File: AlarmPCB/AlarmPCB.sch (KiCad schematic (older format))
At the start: 13 parts

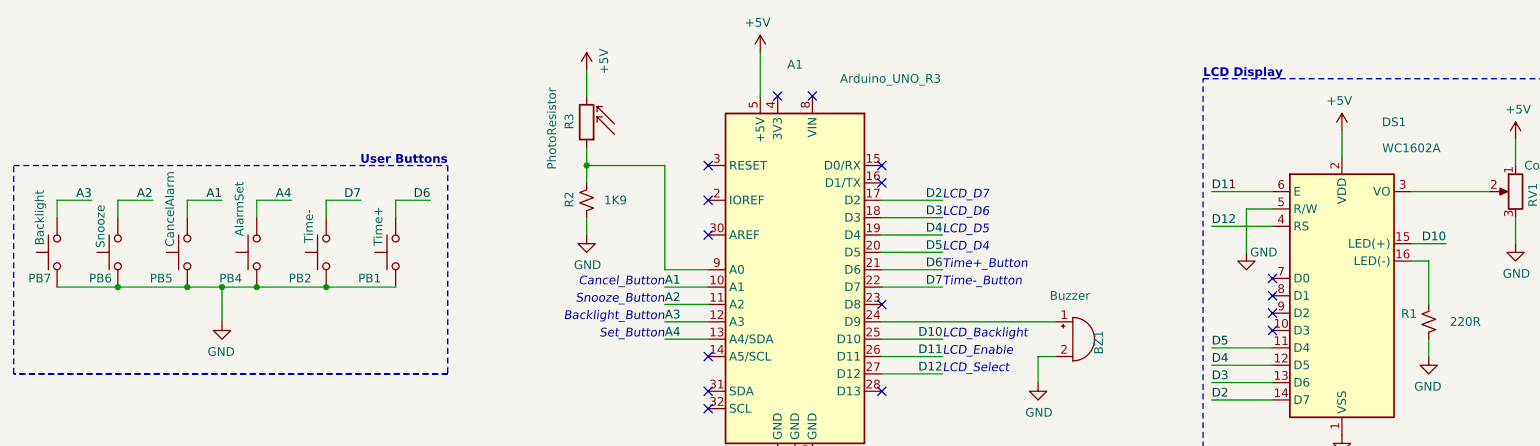
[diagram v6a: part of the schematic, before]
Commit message: Fixed push-button numbering
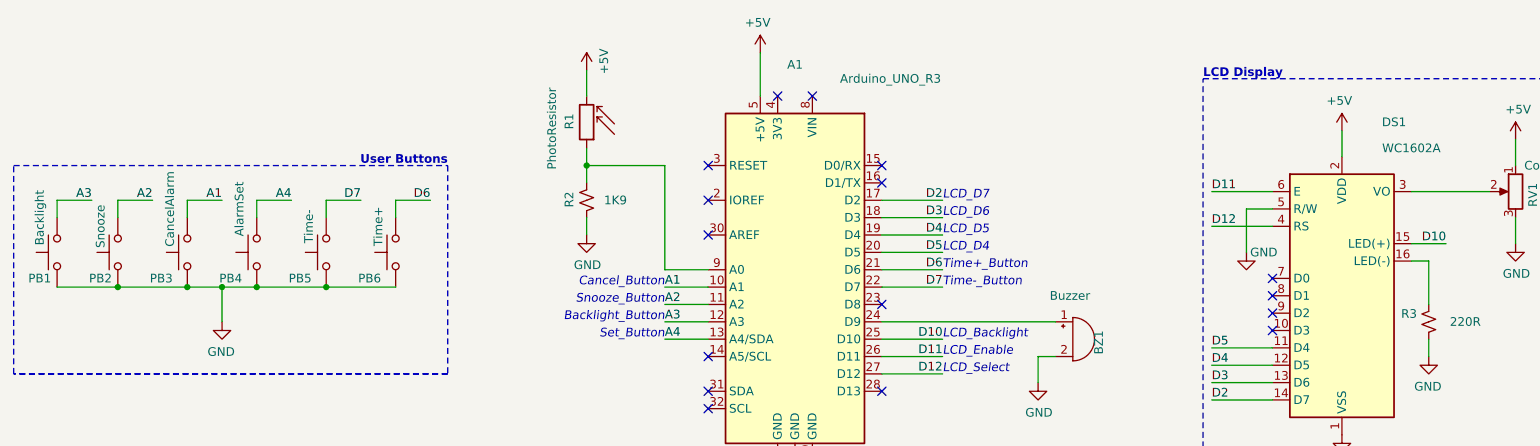
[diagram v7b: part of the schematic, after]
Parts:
- renumbered PB7 to PB1, PB6 to PB2, PB5 to PB3, PB2 to PB5, PB1 to PB6, R3 to R1, R1 to R3
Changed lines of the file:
@@
 EESchema Schematic File Version 4
+LIBS:AlarmPCB-cache
 EELAYER 30 0
 EELAYER END
@@
 $EndComp
 $Comp
-L power:GND #PWR03
+L power:GND #PWR05
 U 1 1 5EFFE387
 P 5250 5100
-F 0 "#PWR03" H 5250 4850 50  0001 C CNN
+F 0 "#PWR05" H 5250 4850 50  0001 C CNN
 F 1 "GND" H 5255 4927 50  0000 C CNN
 F 2 "" H 5250 5100 50  0001 C CNN
@@
 $EndComp
 $Comp
-L power:GND #PWR02
+L power:GND #PWR09
 U 1 1 5F06DAC4
 P 8400 4800
-F 0 "#PWR02" H 8400 4550 50  0001 C CNN
+F 0 "#PWR09" H 8400 4550 50  0001 C CNN
 F 1 "GND" H 8405 4627 50  0000 C CNN
 F 2 "" H 8400 4800 50  0001 C CNN
@@
 $EndComp
 $Comp
-L power:+5V #PWR01
+L power:+5V #PWR08
 U 1 1 5F06E403
 P 8400 3050
-F 0 "#PWR01" H 8400 2900 50  0001 C CNN
+F 0 "#PWR08" H 8400 2900 50  0001 C CNN
 F 1 "+5V" H 8415 3223 50  0000 C CNN
 F 2 "" H 8400 3050 50  0001 C CNN
@@
 	7850 3500 7850 3750
 $Comp
-L power:GND #PWR05
+L power:GND #PWR07
 U 1 1 5F070A81
 P 7850 3750
-F 0 "#PWR05" H 7850 3500 50  0001 C CNN
+F 0 "#PWR07" H 7850 3500 50  0001 C CNN
 F 1 "GND" H 7750 3750 50  0000 C CNN
 F 2 "" H 7850 3750 50  0001 C CNN
@@
 	8900 3800 8900 4050
 $Comp
-L Device:R_Small_US R1
+L Device:R_Small_US R3
 U 1 1 5F073E17
 P 8900 4150
-F 0 "R1" H 8968 4196 50  0000 L CNN
+F 0 "R3" H 8968 4196 50  0000 L CNN
 F 1 "220R" H 8600 4150 50  0000 L CNN
 F 2 "Resistor_THT:R_Axial_DIN0309_L9.0mm_D3.2mm_P12.70mm_Horizontal" H 8900 4150 50  0001 C CNN
@@
 $EndComp
 $Comp
-L power:GND #PWR07
+L power:GND #PWR010
 U 1 1 5F075220
 P 8900 4350
-F 0 "#PWR07" H 8900 4100 50  0001 C CNN
+F 0 "#PWR010" H 8900 4100 50  0001 C CNN
 F 1 "GND" H 8905 4177 50  0000 C CNN
 F 2 "" H 8900 4350 50  0001 C CNN
@@
 D2
 $Comp
-L Switch:SW_Push PB1
+L Switch:SW_Push PB6
 U 1 1 5F088DBE
 P 2950 3750
-F 0 "PB1" V 3100 3900 50  0000 C CNN
+F 0 "PB6" V 3100 3900 50  0000 C CNN
 F 1 "Time+" H 2800 3850 50  0000 C CNN
 F 2 "Button_Switch_THT:Push_E-Switch_KS01Q01" H 2950 3950 50  0001 C CNN
@@
 $EndComp
 $Comp
-L Switch:SW_Push PB2
+L Switch:SW_Push PB5
 U 1 1 5F08BB18
 P 2550 3750
-F 0 "PB2" V 2700 3900 50  0000 C CNN
+F 0 "PB5" V 2700 3900 50  0000 C CNN
 F 1 "Time-" H 2400 3850 50  0000 C CNN
 F 2 "Button_Switch_THT:Push_E-Switch_KS01Q01" H 2550 3950 50  0001 C CNN
@@
 $EndComp
 $Comp
-L Switch:SW_Push PB5
+L Switch:SW_Push PB3
 U 1 1 5F08C740
 P 1750 3750
-F 0 "PB5" V 1900 3900 50  0000 C CNN
+F 0 "PB3" V 1900 3900 50  0000 C CNN
 F 1 "CancelAlarm" H 1500 3850 50  0000 C CNN
 F 2 "Button_Switch_THT:Push_E-Switch_KS01Q01" H 1750 3950 50  0001 C CNN
@@
 $EndComp
 $Comp
-L Switch:SW_Push PB6
+L Switch:SW_Push PB2
 U 1 1 5F08C9FC
 P 1350 3750
-F 0 "PB6" V 1500 3850 50  0000 C CNN
+F 0 "PB2" V 1500 3850 50  0000 C CNN
 F 1 "Snooze" H 1200 3850 50  0000 C CNN
 F 2 "Button_Switch_THT:Push_E-Switch_KS01Q01" H 1350 3950 50  0001 C CNN
@@
 $EndComp
 $Comp
-L Switch:SW_Push PB7
+L Switch:SW_Push PB1
 U 1 1 5F08CE62
 P 1000 3750
-F 0 "PB7" V 1150 3850 50  0000 C CNN
+F 0 "PB1" V 1150 3850 50  0000 C CNN
 F 1 "Backlight" H 800 3850 50  0000 C CNN
 F 2 "Button_Switch_THT:Push_E-Switch_KS01Q01" H 1000 3950 50  0001 C CNN
@@
 	9000 3700 8800 3700
 $Comp
-L power:GND #PWR0101
+L power:GND #PWR012
 U 1 1 5F0AF103
 P 9400 3700
-F 0 "#PWR0101" H 9400 3450 50  0001 C CNN
+F 0 "#PWR012" H 9400 3450 50  0001 C CNN
 F 1 "GND" H 9405 3527 50  0000 C CNN
 F 2 "" H 9400 3700 50  0001 C CNN
@@
 	9400 3700 9400 3550
 $Comp
-L power:+5V #PWR0102
+L power:+5V #PWR011
 U 1 1 5F0B0F52
 P 9400 3100
-F 0 "#PWR0102" H 9400 2950 50  0001 C CNN
+F 0 "#PWR011" H 9400 2950 50  0001 C CNN
 F 1 "+5V" H 9415 3273 50  0000 C CNN
 F 2 "" H 9400 3100 50  0001 C CNN
@@
 	4050 3550 4050 3650
 $Comp
-L Device:R_PHOTO R3
+L Device:R_PHOTO R1
 U 1 1 5F0F643D
 P 4050 3000
-F 0 "R3" V 4150 2950 50  0000 L CNN
+F 0 "R1" V 4150 2950 50  0000 L CNN
 F 1 "PhotoResistor" V 4250 2800 50  0000 L CNN
 F 2 "OptoDevice:R_LDR_4.9x4.2mm_P2.54mm_Vertical" V 4100 2750 50  0001 L CNN
@@
 $EndComp
 $Comp
-L power:+5V #PWR011
+L power:+5V #PWR02
 U 1 1 5F0FF000
 P 4050 2700
-F 0 "#PWR011" H 4050 2550 50  0001 C CNN
+F 0 "#PWR02" H 4050 2550 50  0001 C CNN
 F 1 "+5V" V 4150 2750 50  0000 C CNN
 F 2 "" H 4050 2700 50  0001 C CNN
@@
 	4050 2700 4050 2850
 $Comp
-L power:GND #PWR0103
+L power:GND #PWR03
 U 1 1 5F0D1E03
 P 4050 3650
-F 0 "#PWR0103" H 4050 3400 50  0001 C CNN
+F 0 "#PWR03" H 4050 3400 50  0001 C CNN
 F 1 "GND" H 4055 3477 50  0000 C CNN
 F 2 "" H 4050 3650 50  0001 C CNN
@@
 	1950 3950 2150 3950
 $Comp
-L power:GND #PWR0104
+L power:GND #PWR01
 U 1 1 5F1394E5
 P 1950 4150
-F 0 "#PWR0104" H 1950 3900 50  0001 C CNN
+F 0 "#PWR01" H 1950 3900 50  0001 C CNN
 F 1 "GND" H 1955 3977 50  0000 C CNN
 F 2 "" H 1950 4150 50  0001 C CNN
